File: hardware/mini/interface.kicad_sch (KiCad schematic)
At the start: 41 parts, among them J3 FPC_12P_TOP_CONTACT, SW1 SKPMAME010, SW11 SKPMAME010, SW2 SKPMAME010, SW3 SKPMAME010, SW4 SKPMAME010, SW5 SKPMAME010, SW6 SKPMAME010, SW7 SKPMAME010, SW8 SKPMAME010, SW9 SKPMAME010

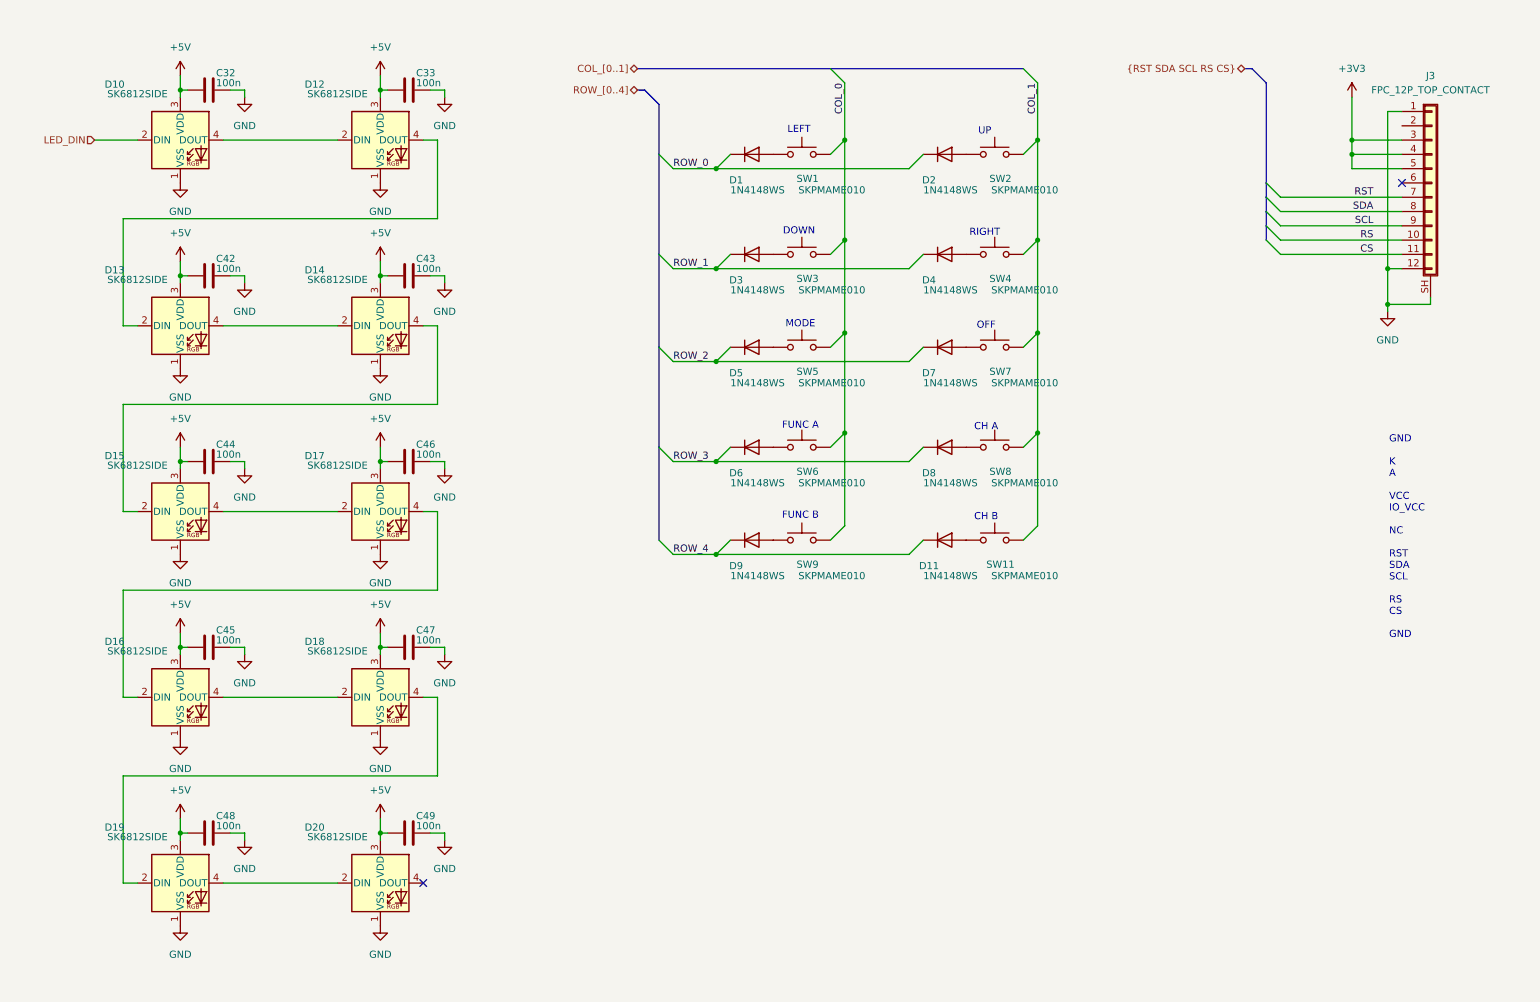
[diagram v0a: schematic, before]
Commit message: finalize parts in schematic
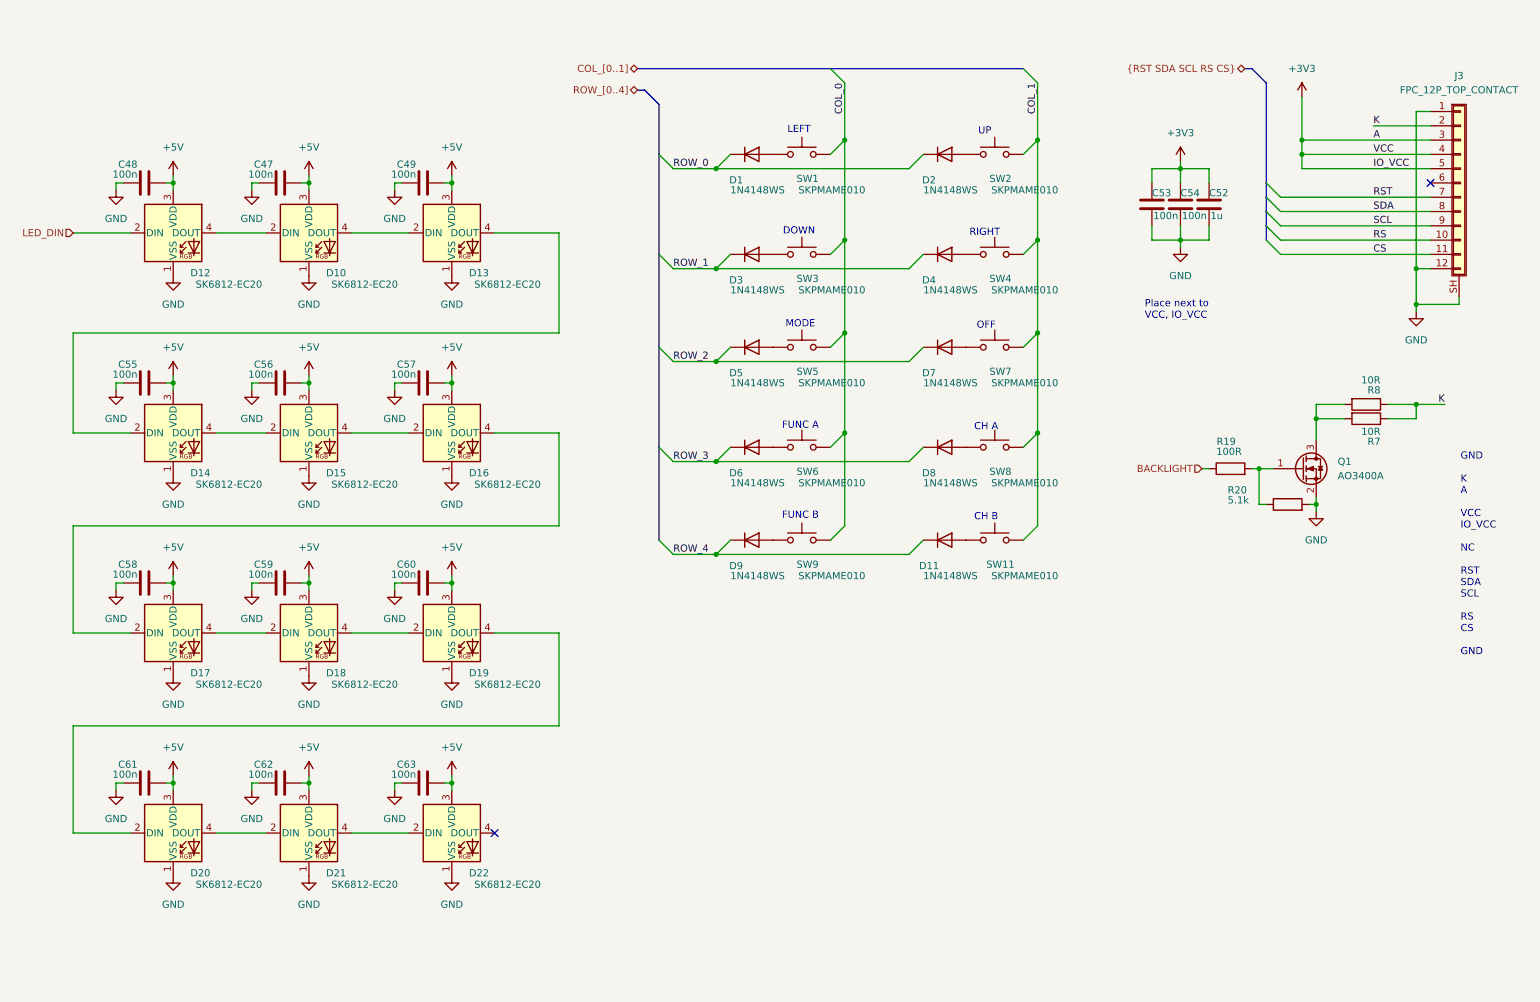
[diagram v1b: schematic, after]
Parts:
- removed C32, C33, C42, C43, C44, C45, C46: 100n, Capacitor_SMD:C_0402_1005Metric, symbol Device:C
- added C52: 1u, Capacitor_SMD:C_1206_3216Metric, symbol Device:C
- added C53, C54, C55, C56, C57, C58, C59, C60, C61, C62, C63: 100n, Capacitor_SMD:C_0402_1005Metric, symbol Device:C
- added D21, D22: SK6812-EC20, LED_SMD:LED_SK6812_PLCC4_5.0x5.0mm_P3.2mm, symbol LED:SK6812
- added Q1: AO3400A, Package_TO_SOT_SMD:SOT-23-3, symbol Transistor_FET:Q_NMOS_GSD
- added R19: 100R, Resistor_SMD:R_0402_1005Metric, symbol Device:R
- added R20: 5.1k, symbol Device:R
- added R7, R8: 10R, Resistor_SMD:R_0402_1005Metric, symbol Device:R
- D10, D12, D13, D14, D15, D16, D17, D18, D19, D20: value SK6812SIDE -> SK6812-EC20
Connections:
- net +3V3: now also C52.1, C53.1, C54.1
- net +5V: now also C47.2, C48.2, C49.2, C55.2, C56.2, C57.2, C58.2, C59.2, C60.2, C61.2, C62.2, C63.2, D21.3 (VDD), D22.3 (VDD); no longer C47.1, C48.1, C49.1
- net GND: now also C47.1, C48.1, C49.1, C52.2, C53.2, C54.2, C55.1, C56.1, C57.1, C58.1, C59.1, C60.1, C61.1, C62.1, C63.1, D21.1 (VSS), D22.1 (VSS), Q1.2 (S), R20.2; no longer C47.2, C48.2, C49.2
- net LED_DIN: now also D12.2 (DIN); no longer D10.2 (DIN)
- net at D20.4 (DOUT): now also D21.2 (DIN)
- net K: now reaches J3.2 (Pin_2)
- net K: now also R7.1, R8.1
- net at D18.2 (DIN): now also D17.4 (DOUT); no longer D16.4 (DOUT)
- net at D10.4 (DOUT): now also D13.2 (DIN); no longer D12.2 (DIN)
- net at D16.2 (DIN): now also D15.4 (DOUT); no longer D17.4 (DOUT)
- net at D12.4 (DOUT): now also D10.2 (DIN); no longer D13.2 (DIN)
- net at D17.2 (DIN): now also D16.4 (DOUT); no longer D15.4 (DOUT)
- new net: D21.4 (DOUT), D22.2 (DIN)
- new net: Q1.1 (G), R19.2, R20.1
- new net: Q1.3 (D), R7.2, R8.2
- new net BACKLIGHT: R19.1
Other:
- note added: "Place next to VCC, IO_VCC"
- moved on the sheet: J3

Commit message: route most
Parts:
- added Q4: AO3400A, Package_TO_SOT_SMD:SOT-23-3, symbol Transistor_FET:Q_NMOS_GSD
- added R46: 100R, Resistor_SMD:R_0402_1005Metric, symbol Device:R
- added R47: 470R, symbol Device:R
- renumbered C48 to C77, C55 to C78, C58 to C79, C61 to C80, C47 to C81, C56 to C82, C59 to C83, C62 to C84, C49 to C85, C57 to C86, C60 to C87, C63 to C88, C53 to C89, C54 to C90, C52 to C91, D21 to D10, D13 to D11, D16 to D12, D19 to D13, D22 to D14, D1 to D15, D3 to D16, D5 to D17, D6 to D18, D9 to D19, D2 to D20, D4 to D21, D7 to D22, D8 to D23, D11 to D24, D12 to D3, D14 to D4, D17 to D5, D20 to D6, D10 to D7, D15 to D8, D18 to D9, J3 to J2, Q1 to Q3, R19 to R42, R20 to R43, R8 to R44, R7 to R45, SW11 to SW10, SW3 to SW2, SW5 to SW3, SW6 to SW4, SW9 to SW5, SW2 to SW6, SW4 to SW7, SW7 to SW8, SW8 to SW9
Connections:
- net +3V3: now also R46.1
- net +5V: now also R47.1
- net LED_DIN: now also Q4.2 (S); no longer D3.2 (DIN)
- new net: D3.2 (DIN), Q4.3 (D), R47.2
- new net: Q4.1 (G), R46.2
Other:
- moved on the sheet: C77, C78, C79, C80, C81, C82, C83, C84, C85, C86, C87, C88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

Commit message: ERC run
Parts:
- removed Q4: AO3400A, Package_TO_SOT_SMD:SOT-23-3, symbol Transistor_FET:Q_NMOS_GSD
- removed R46: 100R, Resistor_SMD:R_0402_1005Metric, symbol Device:R
- removed R47: 470R, symbol Device:R
- renumbered C77 to C67, C78 to C68, C79 to C69, C80 to C70, C81 to C71, C82 to C72, C83 to C73, C84 to C74, C85 to C75, C86 to C76, C87 to C77, C88 to C78, C89 to C79, C90 to C80, C91 to C81, D3 to D1, D12 to D10, D13 to D11, D14 to D12, D15 to D13, D16 to D14, D17 to D15, D18 to D16, D19 to D17, D20 to D18, D21 to D19, D4 to D2, D22 to D20, D23 to D21, D24 to D22, D5 to D3, D6 to D4, D7 to D5, D8 to D6, D9 to D7, D10 to D8, D11 to D9, J2 to J4, Q3 to Q1, R42 to R37, R43 to R38, R44 to R39, R45 to R40
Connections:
- net +5V is gone; now on net +3V3: C67.2, C68.2, C69.2, C70.2, C71.2, C72.2, C73.2, C74.2, C75.2, C76.2, C77.2, C78.2, D1.3 (VDD), D10.3 (VDD), D11.3 (VDD), D12.3 (VDD), D2.3 (VDD), D3.3 (VDD), D4.3 (VDD), D5.3 (VDD), D6.3 (VDD), D7.3 (VDD), D8.3 (VDD), D9.3 (VDD)
- net LED_DIN: now also D1.2 (DIN)
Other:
- note removed: "GND K A VCC IO_VCC NC RST SDA SCL RS CS GND"
- moved on the sheet: C67, C68, C69, C70, C71, C72, C73, C74, C75, C76, C77, C78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

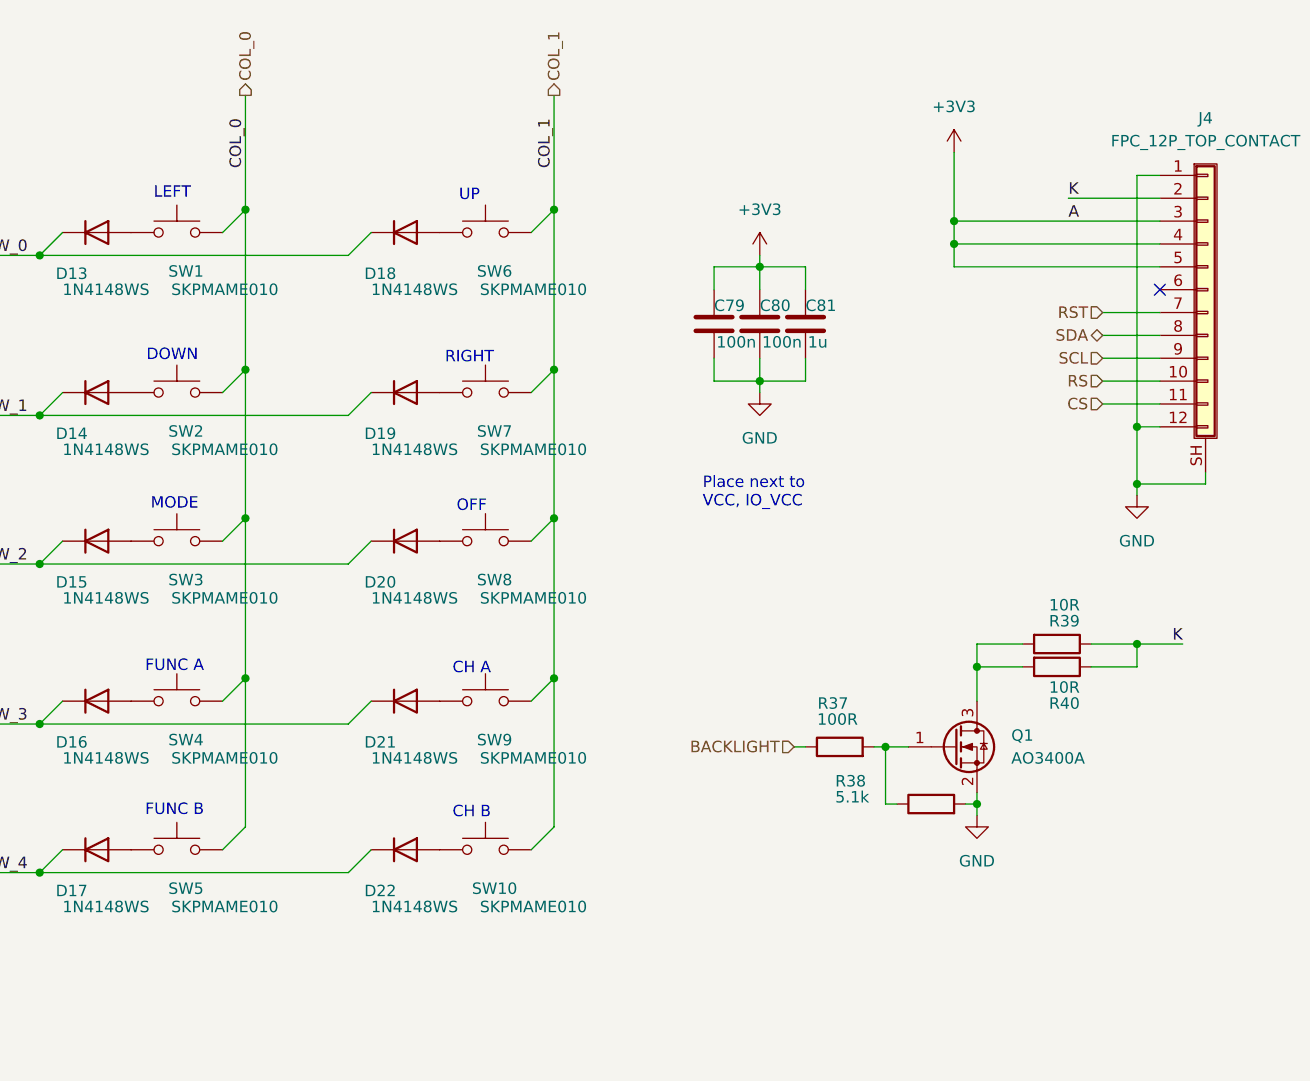
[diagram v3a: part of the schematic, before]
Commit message: assign footprints & LCSC id
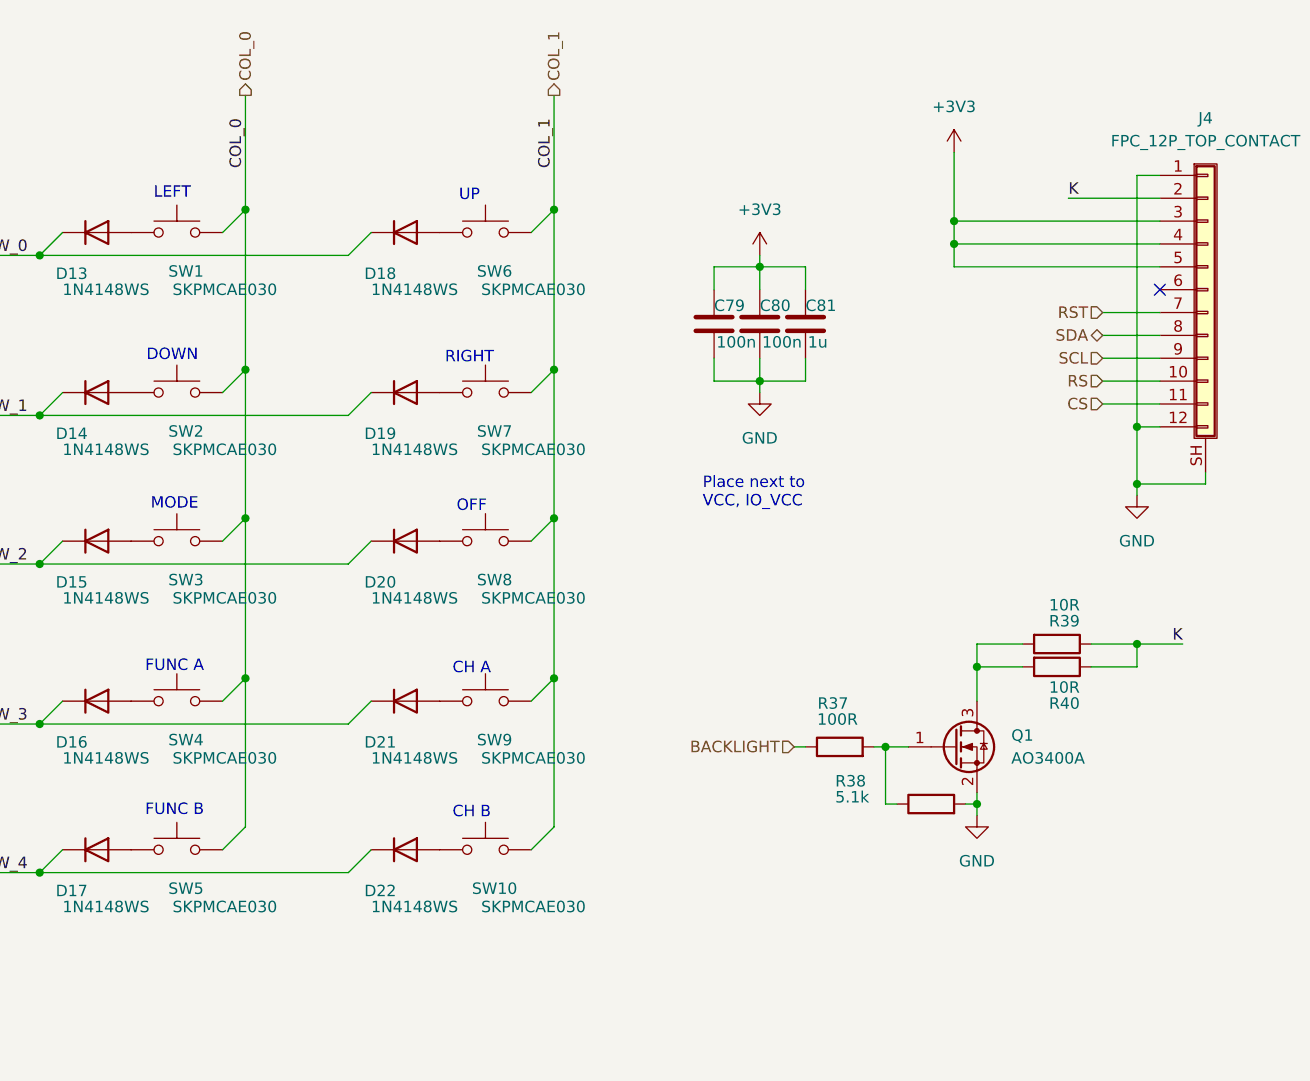
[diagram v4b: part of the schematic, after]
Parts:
- D1, D10, D11, D12, D2, D3, D4, D5, D6, D7, D8, D9: LCSC (none) -> C2909058
- D13, D14, D15, D16, D17, D18, D19, D20, D21, D22: LCSC (none) -> C2128
- J4: LCSC (none) -> C262585
- R38: footprint (none) -> Resistor_SMD:R_0402_1005Metric
- SW1, SW10, SW2, SW3, SW4, SW5, SW6, SW7, SW8, SW9: value SKPMAME010 -> SKPMCAE030; LCSC (none) -> C7430178

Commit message: build all footprints
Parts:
- D1, D10, D11, D12, D2, D3, D4, D5, D6, D7, D8, D9: footprint LED_SMD:LED_SK6812_PLCC4_5.0x5.0mm_P3.2mm -> protovolt_mini_fp:LED_SK6812_EC20_2.0x2.0mm
- J4: footprint (none) -> protovolt_mini_fp:JUSHUO_AFC07-S12ECA-00_1x12-1MP_P0.5mm_Horizontal
- SW1, SW10, SW2, SW3, SW4, SW5, SW6, SW7, SW8, SW9: footprint (none) -> protovolt_mini_fp:SW_PUSH_SKPM_6x5mm
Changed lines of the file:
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@@
 			)
 		)
-		(property "Footprint" "LED_SMD:LED_SK6812_PLCC4_5.0x5.0mm_P3.2mm"
+		(property "Footprint" "protovolt_mini_fp:LED_SK6812_EC20_2.0x2.0mm"
 			(at 73.66 64.77 0)
 			(effects
@@
 			)
 		)
-		(property "Footprint" "LED_SMD:LED_SK6812_PLCC4_5.0x5.0mm_P3.2mm"
+		(property "Footprint" "protovolt_mini_fp:LED_SK6812_EC20_2.0x2.0mm"
 			(at 49.53 171.45 0)
 			(effects
@@
 			)
 		)
-		(property "Footprint" "LED_SMD:LED_SK6812_PLCC4_5.0x5.0mm_P3.2mm"
+		(property "Footprint" "protovolt_mini_fp:LED_SK6812_EC20_2.0x2.0mm"
 			(at 73.66 100.33 0)
 			(effects
@@
 			)
 		)
-		(property "Footprint" ""
+		(property "Footprint" "protovolt_mini_fp:SW_PUSH_SKPM_6x5mm"
 			(at 190.5 92.71 0)
 			(effects
@@
 			)
 		)
-		(property "Footprint" "LED_SMD:LED_SK6812_PLCC4_5.0x5.0mm_P3.2mm"
+		(property "Footprint" "protovolt_mini_fp:LED_SK6812_EC20_2.0x2.0mm"
 			(at 49.53 64.77 0)
 			(effects
@@
 			)
 		)
-		(property "Footprint" "LED_SMD:LED_SK6812_PLCC4_5.0x5.0mm_P3.2mm"
+		(property "Footprint" "protovolt_mini_fp:LED_SK6812_EC20_2.0x2.0mm"
 			(at 73.66 135.89 0)
 			(effects
@@
 			)
 		)
-		(property "Footprint" ""
+		(property "Footprint" "protovolt_mini_fp:JUSHUO_AFC07-S12ECA-00_1x12-1MP_P0.5mm_Horizontal"
 			(at 270.51 69.85 0)
 			(effects
@@
 			)
 		)
-		(property "Footprint" "LED_SMD:LED_SK6812_PLCC4_5.0x5.0mm_P3.2mm"
+		(property "Footprint" "protovolt_mini_fp:LED_SK6812_EC20_2.0x2.0mm"
 			(at 99.06 64.77 0)
 			(effects
@@
 			)
 		)
-		(property "Footprint" ""
+		(property "Footprint" "protovolt_mini_fp:SW_PUSH_SKPM_6x5mm"
 			(at 156.21 127 0)
 			(effects
@@
 			)
 		)
-		(property "Footprint" "LED_SMD:LED_SK6812_PLCC4_5.0x5.0mm_P3.2mm"
+		(property "Footprint" "protovolt_mini_fp:LED_SK6812_EC20_2.0x2.0mm"
 			(at 99.06 171.45 0)
 			(effects
@@
 			)
 		)
-		(property "Footprint" ""
+		(property "Footprint" "protovolt_mini_fp:SW_PUSH_SKPM_6x5mm"
 			(at 190.5 58.42 0)
 			(effects
@@
 			)
 		)
-		(property "Footprint" "LED_SMD:LED_SK6812_PLCC4_5.0x5.0mm_P3.2mm"
+		(property "Footprint" "protovolt_mini_fp:LED_SK6812_EC20_2.0x2.0mm"
 			(at 49.53 135.89 0)
 			(effects
@@
 			)
 		)
-		(property "Footprint" ""
+		(property "Footprint" "protovolt_mini_fp:SW_PUSH_SKPM_6x5mm"
 			(at 156.21 110.49 0)
 			(effects
@@
 			)
 		)
-		(property "Footprint" ""
+		(property "Footprint" "protovolt_mini_fp:SW_PUSH_SKPM_6x5mm"
 			(at 190.5 127 0)
 			(effects
@@
 			)
 		)
-		(property "Footprint" ""
+		(property "Footprint" "protovolt_mini_fp:SW_PUSH_SKPM_6x5mm"
 			(at 156.21 92.71 0)
 			(effects
@@
 			)
 		)
-		(property "Footprint" "LED_SMD:LED_SK6812_PLCC4_5.0x5.0mm_P3.2mm"
+		(property "Footprint" "protovolt_mini_fp:LED_SK6812_EC20_2.0x2.0mm"
 			(at 73.66 171.45 0)
 			(effects
@@
 			)
 		)
-		(property "Footprint" "LED_SMD:LED_SK6812_PLCC4_5.0x5.0mm_P3.2mm"
+		(property "Footprint" "protovolt_mini_fp:LED_SK6812_EC20_2.0x2.0mm"
 			(at 99.06 100.33 0)
 			(effects
@@
 			)
 		)
-		(property "Footprint" ""
+		(property "Footprint" "protovolt_mini_fp:SW_PUSH_SKPM_6x5mm"
 			(at 190.5 110.49 0)
 			(effects
@@
 			)
 		)
-		(property "Footprint" "LED_SMD:LED_SK6812_PLCC4_5.0x5.0mm_P3.2mm"
+		(property "Footprint" "protovolt_mini_fp:LED_SK6812_EC20_2.0x2.0mm"
 			(at 49.53 100.33 0)
 			(effects
@@
 			)
 		)
-		(property "Footprint" ""
+		(property "Footprint" "protovolt_mini_fp:SW_PUSH_SKPM_6x5mm"
 			(at 190.5 76.2 0)
 			(effects
@@
 			)
 		)
-		(property "Footprint" "LED_SMD:LED_SK6812_PLCC4_5.0x5.0mm_P3.2mm"
+		(property "Footprint" "protovolt_mini_fp:LED_SK6812_EC20_2.0x2.0mm"
 			(at 99.06 135.89 0)
 			(effects
@@
 			)
 		)
-		(property "Footprint" ""
+		(property "Footprint" "protovolt_mini_fp:SW_PUSH_SKPM_6x5mm"
 			(at 156.21 58.42 0)
 			(effects
@@
 			)
 		)
-		(property "Footprint" ""
+		(property "Footprint" "protovolt_mini_fp:SW_PUSH_SKPM_6x5mm"
 			(at 156.21 76.2 0)
 			(effects

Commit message: place ui elements
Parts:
- renumbered C71 to C68, C75 to C69, C79 to C70, C80 to C71, C81 to C72, C68 to C73, C72 to C74, C76 to C75, C69 to C76, C73 to C77, C77 to C78, C70 to C79, C74 to C80, C78 to C81, D15 to D11, D20 to D12, D16 to D13, D21 to D14, D3 to D15, D7 to D16, D11 to D17, D17 to D18, D22 to D19, D5 to D2, D4 to D20, D8 to D21, D12 to D22, D9 to D3, D13 to D4, D18 to D5, D14 to D6, D19 to D7, D2 to D8, D6 to D9, R39 to R37, R40 to R38, R37 to R39, R38 to R40, SW6 to SW2, SW2 to SW3, SW7 to SW4, SW3 to SW5, SW8 to SW6, SW4 to SW7, SW9 to SW8, SW5 to SW9

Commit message: route power stage
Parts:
- removed C77, C78, C79, C80, C81: 100n, Capacitor_SMD:C_0402_1005Metric, symbol Device:C
- removed D11, D12, D13, D14, D18, D19, D4, D5, D6, D7: 1N4148WS, Diode_SMD:D_SOD-323, symbol Diode:1N4148WS
- removed D16, D17, D20, D21, D22: SK6812-EC20, protovolt_mini_fp:LED_SK6812_EC20_2.0x2.0mm, symbol LED:SK6812
- removed SW1, SW10, SW2, SW3, SW4, SW5, SW6, SW7, SW8, SW9: SKPMCAE030, protovolt_mini_fp:SW_PUSH_SKPM_6x5mm, symbol Switch:SW_Push
- added D10, D11, D12, D13, D14, D15, D4, D5, D6: 1N4148WS, Diode_SMD:D_SOD-323, symbol Device:D_45deg
- added SW1, SW2, SW3, SW4, SW5, SW6, SW7, SW8, SW9: SKPMCAE030, protovolt_mini_fp:SW_PUSH_SKPM_6x5mm, symbol Switch:SW_Push_45deg
- renumbered D15 to D16, D8 to D7, D9 to D8, D10 to D9
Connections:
- net COL_0: now also SW1.2, SW4.2, SW7.2
- net COL_1: now also SW2.2, SW5.2, SW8.2
- net ROW_0: now also D4.1 (K), D5.1 (K), D6.1 (K)
- net ROW_1: now also D10.1 (K), D11.1 (K), D12.1 (K)
- net ROW_2: now also D13.1 (K), D14.1 (K), D15.1 (K)
- new net: D15.2 (A), SW9.1
- new net: D5.2 (A), SW2.1
- new net: D10.2 (A), SW4.1
- new net: D14.2 (A), SW8.1
- new net: D6.2 (A), SW3.1
- new net: D12.2 (A), SW6.1
- new net: D13.2 (A), SW7.1
- new net: D4.2 (A), SW1.1
- new net: D11.2 (A), SW5.1
- new net COL_2: SW3.2, SW6.2, SW9.2
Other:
- note removed: "CH A"
- note removed: "CH B"
- note removed: "DOWN"
- note removed: "FUNC A"
- note removed: "FUNC B"
- note removed: "LEFT"
- note removed: "MODE"
- note removed: "OFF"
- note removed: "RIGHT"
- note removed: "UP"

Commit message: route digitals
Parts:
- C72: footprint Capacitor_SMD:C_1206_3216Metric -> Capacitor_SMD:C_0603_1608Metric; LCSC C1848 -> C15849
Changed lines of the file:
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@@
 			)
 		)
-		(property "Footprint" "Capacitor_SMD:C_1206_3216Metric"
+		(property "Footprint" "Capacitor_SMD:C_0603_1608Metric"
 			(at 227.0252 77.47 0)
 			(effects
@@
 			)
 		)
-		(property "LCSC" "C1848"
+		(property "LCSC" "C15849"
 			(at 226.06 73.66 0)
 			(effects
